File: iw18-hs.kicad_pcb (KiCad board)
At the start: 2 copper layers, 115 parts, among them J1 USB_C_Receptacle_USB2.0_14P, Q1 Q_NMOS_GSD, Q2 Q_NMOS_GDS, SW1 SW_SPST, SW2 SW_SPDT, U1 IV-18, U10 TXS0104EPW, U11 MAX811TEUS-T, U12 AT24CS08-STUM, U13 MQ-6, U14 BME680, U15 LSM6DS3, U2 BQ25895RTW, U3 ESP32-C6-WROOM-1, U4 LM1117DT-3.3, U5 MCP4017-xxxxLT, U6 TPS25751DREFR_C30169739, U7 LM3478MA, U8 USBLC6-2P6, U9 DRV8837

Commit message: Component changes, some new feature
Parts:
- removed C15: 10uF, Capacitor_SMD:CP_Elec_5x4.5
- added C52: 10uF, Capacitor_SMD:C_1206_3216Metric, F.Cu at (187.2, 128.0)
- added R6: 10k, Resistor_SMD:R_0805_2012Metric, F.Cu at (161.0, 136.5)
- added U16: 74LVC1G125, Package_TO_SOT_SMD:Texas_R-PDSO-G5_DCK-5, F.Cu at (161.1, 133.2)
- C13, C16, C51: value 150uF -> 100uF; footprint Capacitor_SMD:CP_Elec_5x4.5 -> Capacitor_SMD:C_1206_3216Metric
- C17, C21, C22, C24, C25, C32, C34: footprint Capacitor_SMD:C_0805_2012Metric -> Capacitor_SMD:C_0402_1005Metric
- C4: value 50uF -> 47uF
- D1: value SS14-DC -> SBA120CS-R1; footprint Diode_SMD:D_SMA -> Diode_SMD:D_SOD-323
- D4: value B3100BE-13 -> SDB160WS-AQ-DIO; footprint Diode_SMD:D_SMB -> Diode_SMD:D_SOD-323
- L1: value L -> 100uH; footprint Inductor_SMD:L_1812_4532Metric -> Inductor_SMD:L_0805_2012Metric
- L2: value 47uF -> 100uH
- L3: value 2.2uF -> 2.2uH; footprint Inductor_SMD:L_Bourns_SRP1038C_10.0x10.0mm -> Inductor_SMD:L_Taiyo-Yuden_NR-50xx
- Q2: footprint Package_TO_SOT_SMD:TO-263-2 -> Package_TO_SOT_SMD:TO-252-3_TabPin2
- R10: value 2.7k -> 10k
- R31, R32: footprint Resistor_SMD:R_0805_2012Metric -> Resistor_SMD:R_0402_1005Metric
- U4: footprint Package_TO_SOT_SMD:TO-252-3_TabPin2 -> Package_TO_SOT_SMD:SOT-223-3_TabPin2
- moved U13 106.1 mm to (64.6, 24.6)
- moved J1 97.5 mm to (28.9, 106.2), turned to -90 degrees
- moved R16 87.9 mm to (35.9, 102.7), turned to 0 degrees
- moved U8 87.6 mm to (35.9, 105.1), turned to 0 degrees
- moved R15 87.5 mm to (35.8, 107.7), turned to 0 degrees
- moved F1 87.4 mm to (35.9, 110.0), turned to 0 degrees
- moved C18 46.8 mm to (55.3, 141.6)
- moved C23 46.8 mm to (59.0, 137.1)
- moved R19 46.8 mm to (51.6, 137.1)
- moved R22 46.8 mm to (55.3, 137.1)
- moved R28 46.8 mm to (55.3, 139.3)
- moved R29 46.8 mm to (46.3, 138.9)
- moved R30 46.8 mm to (46.3, 141.1)
- moved BT1 46.8 mm to (50.0, 67.2)
- moved C19 46.8 mm to (48.5, 95.6)
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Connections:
- U3 pad 15: ETANOL_SENSOR_HEAT -> unconnected-(U3-GPIO9-Pad15)
- U3 pad 27: unconnected-(U3-GPIO2/ADC1_CH2-Pad27) -> ETANOL_SENSOR_HEAT
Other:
- board outline added: 40 x 120.8 mm

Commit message: plytka wip
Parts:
- added J2: Conn_02x10_Counter_Clockwise, Connector_PinHeader_2.54mm:PinHeader_2x10_P2.54mm_Vertical, F.Cu at (33.8, 67.0)
- added J3: Conn_02x10_Counter_Clockwise, Connector_PinSocket_2.54mm:PinSocket_2x10_P2.54mm_Horizontal, F.Cu at (33.6, 49.5)
- moved C51 222.4 mm to (36.0, 150.0)
- moved L1 221.1 mm to (34.8, 146.8)
- moved TP5 220.3 mm to (30.2, 149.8)
- moved C13 217.6 mm to (33.5, 150.0)
- moved C12 214.7 mm to (32.0, 153.8)
- moved U4 213.7 mm to (31.0, 159.5)
- moved C11 204.8 mm to (28.5, 153.2)
- moved C4 204.2 mm to (26.0, 153.2)
- moved TP4 154.8 mm to (49.7, 122.3), turned to 180 degrees
- moved C3 148.0 mm to (49.7, 119.0), turned to 90 degrees
- moved C14 144.7 mm to (62.2, 78.8), turned to -90 degrees
- moved U5 144.0 mm to (60.0, 79.0), turned to -90 degrees
- moved TP1 142.8 mm to (63.5, 83.8), turned to 90 degrees
- moved R10 141.6 mm to (48.2, 90.8)
- moved C52 140.7 mm to (53.7, 83.8), turned to 0 degrees
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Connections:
- net /. renamed /VFD/.
- net /A renamed /VFD/A
- net /B renamed /VFD/B
- net /C renamed /VFD/C
- net /D renamed /VFD/D
- net /D1 renamed /VFD/D1
- net /D2 renamed /VFD/D2
- net /D3 renamed /VFD/D3
- net /D4 renamed /VFD/D4
- net /D5 renamed /VFD/D5
- net /D6 renamed /VFD/D6
- net /D7 renamed /VFD/D7
- net /D8 renamed /VFD/D8
- net /D9 renamed /VFD/D9
- net /E renamed /VFD/E
- net /F renamed /VFD/F
- net /G renamed /VFD/G
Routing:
- net /VFD/D5: track 0.00 -> 83.9 mm, vias 0 -> 1
- net /VFD/D3: track 0.00 -> 73.9 mm, vias 0 -> 1
- net /VFD/D4: track 0.00 -> 65.4 mm, vias 0 -> 2
- net /VFD/D1: track 0.00 -> 63.1 mm, vias 0 -> 1
- net /VFD/D2: track 0.00 -> 52.4 mm, vias 0 -> 2
- net /VFD/F: track 0.00 -> 51.1 mm, vias 0 -> 2
- net /VFD/G: track 0.00 -> 40.5 mm, vias 0 -> 2
- net HEATER_A: track 0.00 -> 36.9 mm, vias 0 -> 2
- net /VFD/.: track 0.00 -> 35.9 mm, vias 0 -> 2
- net GND: track 0.00 -> 5.26 mm
- net Net-(U2-REGN): track 0.00 -> 2.28 mm
- net VSYS: track 0.00 -> 0.50 mm
- net Net-(SW2-B): track 0.00 -> 0.50 mm
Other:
- board size 40 x 120.8 mm -> 40 x 159.5 mm
- board text added: "Do ogarnięcia pozycjonowanie. na razie wys 18mm+10mm+10mm, szer 40mm czy aby na pewno dobra kolejnosc pinów? będziemy pewnie od tyłu robić."

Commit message: components moved
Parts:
- moved C39 6.26 mm to (84.3, 146.7)
- moved C40 6.26 mm to (84.2, 127.3)
- moved C41 6.26 mm to (84.9, 108.6)
- moved C45 6.26 mm to (84.4, 90.1)
- moved D3 6.26 mm to (79.9, 146.6)
- moved D5 6.26 mm to (79.9, 127.5)
- moved D6 6.26 mm to (80.2, 108.8)
- moved D7 6.26 mm to (80.0, 90.5)
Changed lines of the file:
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@@
 	(footprint "Capacitor_SMD:C_0805_2012Metric"
 		(layer "F.Cu")
-		(at 89.9 87.1 -90)
+		(at 84.4 90.1 -90)
 		(descr "Capacitor SMD 0805 (2012 Metric), square (rectangular) end terminal, IPC-7351 nominal, (Body size source: IPC-SM-782 page 76, https://www.pcb-3d.com/wordpress/wp-content/uploads/ipc-sm-782a_amendment_1_and_2.pdf, https://docs.google.com/spreadsheets/d/1BsfQQcO9C6DZCsRaXUlFlo91Tg2WpOkGARC1WS5S8t0/edit?usp=sharing)")
 		(tags "capacitor")
@@
 	(footprint "LED_SMD:LED_WS2812B_PLCC4_5.0x5.0mm_P3.2mm"
 		(layer "F.Cu")
-		(at 85.4 124.5 -90)
+		(at 79.9 127.5 -90)
 		(descr "5.0mm x 5.0mm Addressable RGB LED NeoPixel, https://cdn-shop.adafruit.com/datasheets/WS2812B.pdf")
 		(tags "LED RGB NeoPixel PLCC-4 5050")
@@
 	(footprint "LED_SMD:LED_WS2812B_PLCC4_5.0x5.0mm_P3.2mm"
 		(layer "F.Cu")
-		(at 85.5 87.5 -90)
+		(at 80 90.5 -90)
 		(descr "5.0mm x 5.0mm Addressable RGB LED NeoPixel, https://cdn-shop.adafruit.com/datasheets/WS2812B.pdf")
 		(tags "LED RGB NeoPixel PLCC-4 5050")
@@
 	(footprint "Capacitor_SMD:C_0805_2012Metric"
 		(layer "F.Cu")
-		(at 89.8 143.7 -90)
+		(at 84.3 146.7 -90)
 		(descr "Capacitor SMD 0805 (2012 Metric), square (rectangular) end terminal, IPC-7351 nominal, (Body size source: IPC-SM-782 page 76, https://www.pcb-3d.com/wordpress/wp-content/uploads/ipc-sm-782a_amendment_1_and_2.pdf, https://docs.google.com/spreadsheets/d/1BsfQQcO9C6DZCsRaXUlFlo91Tg2WpOkGARC1WS5S8t0/edit?usp=sharing)")
 		(tags "capacitor")
@@
 	(footprint "LED_SMD:LED_WS2812B_PLCC4_5.0x5.0mm_P3.2mm"
 		(layer "F.Cu")
-		(at 85.75 105.85 -90)
+		(at 80.25 108.85 -90)
 		(descr "5.0mm x 5.0mm Addressable RGB LED NeoPixel, https://cdn-shop.adafruit.com/datasheets/WS2812B.pdf")
 		(tags "LED RGB NeoPixel PLCC-4 5050")
@@
 	(footprint "Capacitor_SMD:C_0805_2012Metric"
 		(layer "F.Cu")
-		(at 90.4 105.6 -90)
+		(at 84.9 108.6 -90)
 		(descr "Capacitor SMD 0805 (2012 Metric), square (rectangular) end terminal, IPC-7351 nominal, (Body size source: IPC-SM-782 page 76, https://www.pcb-3d.com/wordpress/wp-content/uploads/ipc-sm-782a_amendment_1_and_2.pdf, https://docs.google.com/spreadsheets/d/1BsfQQcO9C6DZCsRaXUlFlo91Tg2WpOkGARC1WS5S8t0/edit?usp=sharing)")
 		(tags "capacitor")
@@
 	(footprint "Capacitor_SMD:C_0805_2012Metric"
 		(layer "F.Cu")
-		(at 89.65 124.3 -90)
+		(at 84.15 127.3 -90)
 		(descr "Capacitor SMD 0805 (2012 Metric), square (rectangular) end terminal, IPC-7351 nominal, (Body size source: IPC-SM-782 page 76, https://www.pcb-3d.com/wordpress/wp-content/uploads/ipc-sm-782a_amendment_1_and_2.pdf, https://docs.google.com/spreadsheets/d/1BsfQQcO9C6DZCsRaXUlFlo91Tg2WpOkGARC1WS5S8t0/edit?usp=sharing)")
 		(tags "capacitor")
@@
 	(footprint "LED_SMD:LED_WS2812B_PLCC4_5.0x5.0mm_P3.2mm"
 		(layer "F.Cu")
-		(at 85.4 143.55 -90)
+		(at 79.9 146.55 -90)
 		(descr "5.0mm x 5.0mm Addressable RGB LED NeoPixel, https://cdn-shop.adafruit.com/datasheets/WS2812B.pdf")
 		(tags "LED RGB NeoPixel PLCC-4 5050")
@@
 	)
 	(gr_text "Do ogarnięcia pozycjonowanie. na razie wys 18mm+10mm+10mm, szer 40mm\nczy aby na pewno dobra kolejnosc pinów? będziemy pewnie od tyłu robić."
-		(at 8.75 58.75 0)
+		(at 13 59.75 0)
 		(layer "F.Fab")
 		(effects

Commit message: Do compoent placing
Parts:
- added BT2: 247, 247:BAT_247, B.Cu at (111.4, 101.6)
- added J4: Conn_02x08_Odd_Even, Connector_PinHeader_2.54mm:PinHeader_2x08_P2.54mm_Vertical, F.Cu at (214.2, 110.3)
- added J5: Conn_02x08_Odd_Even, Connector_PinHeader_2.54mm:PinHeader_2x08_P2.54mm_Vertical, F.Cu at (208.1, 110.3)
- BT1: value Battery_Cell -> 247; footprint Battery:BatteryHolder_MPD_BH-18650-PC -> 247:BAT_247
- U13: moved to B.Cu
- moved C26 165.7 mm to (177.9, 93.3), turned to 180 degrees
- moved U3 159.0 mm to (189.9, 100.3), turned to 0 degrees
- moved C28 148.6 mm to (164.8, 109.9), turned to 0 degrees
- moved U8 141.8 mm to (175.2, 89.6)
- moved R30 140.2 mm to (169.6, 95.7), turned to 0 degrees
- moved U13 139.4 mm to (241.1, 105.2), turned to 90 degrees
- moved C4 137.1 mm to (153.7, 103.4)
- moved C11 136.7 mm to (155.8, 103.4)
- moved R5 136.6 mm to (224.7, 110.2), turned to 0 degrees
- moved R7 136.2 mm to (177.9, 113.3), turned to 90 degrees
- moved R29 136.2 mm to (166.1, 95.7)
- moved U11 136.1 mm to (172.9, 96.5), turned to 180 degrees
- moved R26 134.7 mm to (177.9, 109.9), turned to -90 degrees
- moved C12 133.7 mm to (158.0, 108.9)
- moved Q1 131.6 mm to (224.2, 106.6), turned to 180 degrees
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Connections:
- SW2 pad 3: Net-(BT1-+) -> Net-(SW2-C)
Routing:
- net /VFD/D5: track 83.9 -> 0.00 mm, vias 1 -> 0
- net /VFD/D3: track 73.9 -> 0.00 mm, vias 1 -> 0
- net /VFD/D4: track 65.4 -> 0.00 mm, vias 2 -> 0
- net /VFD/D1: track 63.1 -> 0.00 mm, vias 1 -> 0
- net /VFD/D2: track 52.4 -> 0.00 mm, vias 2 -> 0
- net /VFD/F: track 51.1 -> 0.00 mm, vias 2 -> 0
- net /VFD/G: track 40.5 -> 0.00 mm, vias 2 -> 0
- net HEATER_A: track 36.9 -> 0.00 mm, vias 2 -> 0
- net /VFD/.: track 35.9 -> 0.00 mm, vias 2 -> 0
- net GND: track 5.26 -> 0.00 mm
- net Net-(U2-REGN): track 2.28 -> 0.00 mm
- net VSYS: track 0.50 -> 0.00 mm
- net Net-(SW2-B): track 0.50 -> 0.00 mm
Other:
- board size 40 x 159.5 mm -> 204.4 x 40 mm
- board text removed: "Periph"
- board text removed: "Power"

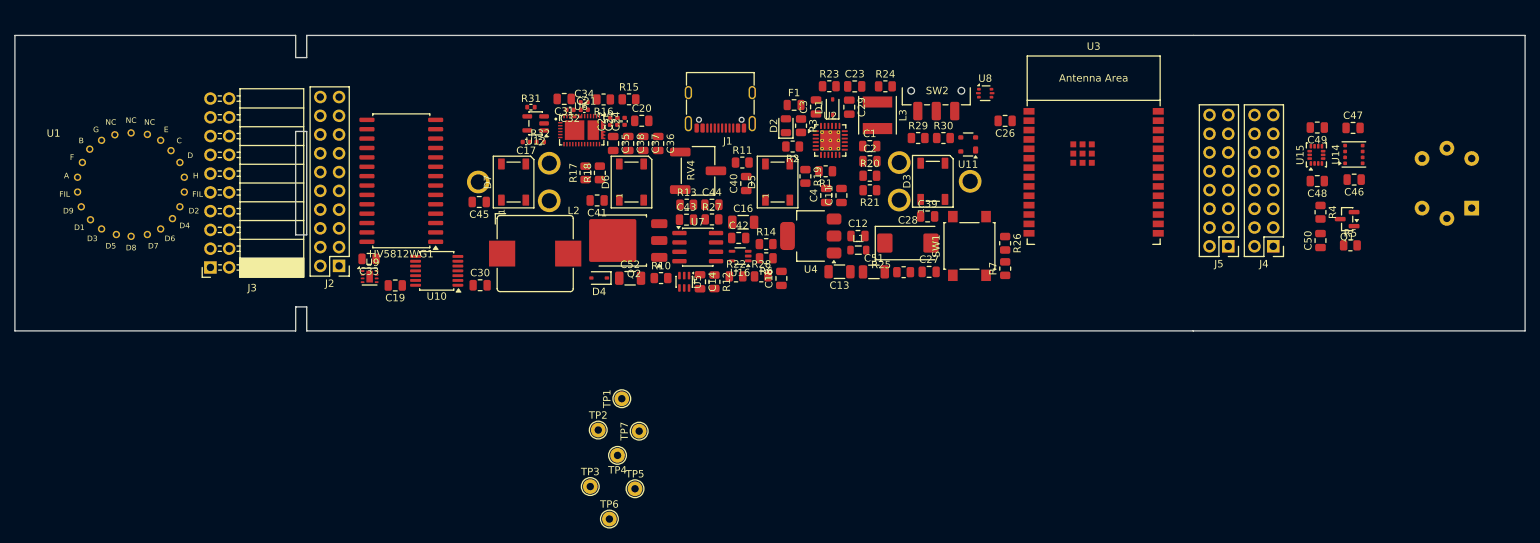
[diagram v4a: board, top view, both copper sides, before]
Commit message: Refine board
* Add UART connector for chaining and controll
* shrink the board
workspace 1 output DP-6
* allow for pd controller eeprom programming
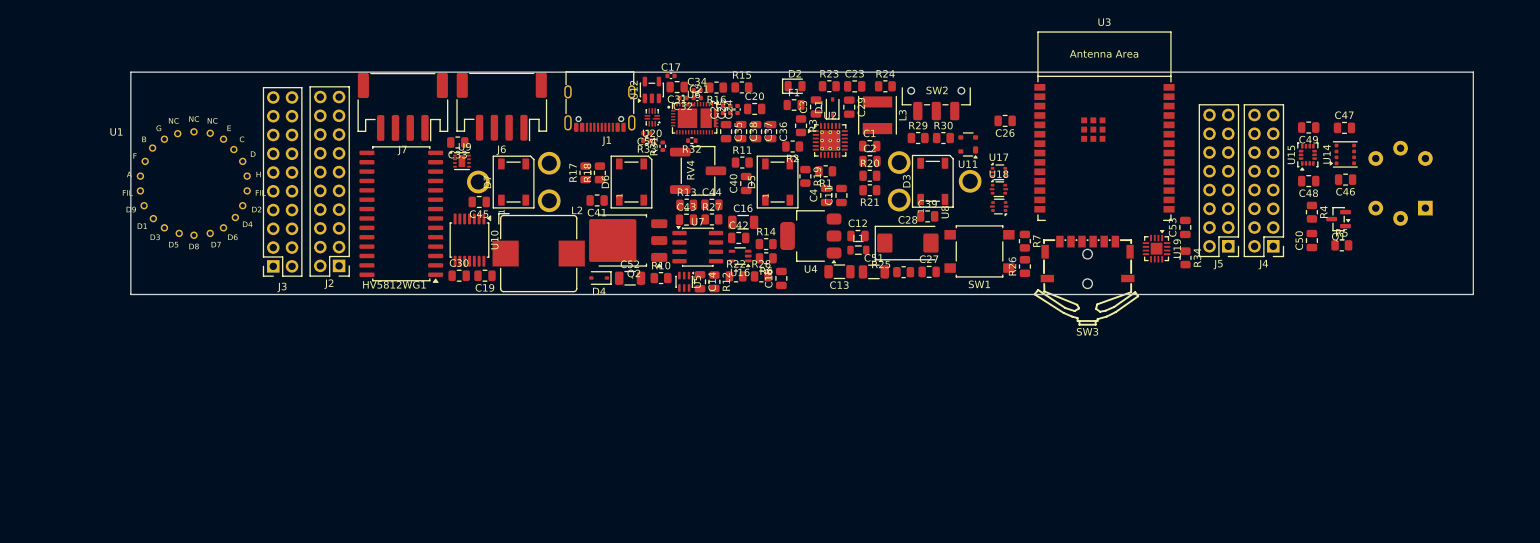
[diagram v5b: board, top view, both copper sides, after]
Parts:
- removed TP1, TP2, TP3, TP4, TP5, TP6, TP7: TestPoint_Probe, TestPoint:TestPoint_THTPad_D2.0mm_Drill1.0mm
- added C53: 100nF, Capacitor_SMD:C_0805_2012Metric, F.Cu at (202.3, 107.8)
- added C54: 100nF, Capacitor_SMD:C_0402_1005Metric, F.Cu at (129.4, 95.0)
- added J6: Conn_01x04_MountingPin, Connector_JST:JST_PH_S4B-PH-SM4-TB_1x04-1MP_P2.00mm_Horizontal, F.Cu at (109.8, 91.4)
- added J7: Conn_01x04_MountingPin, Connector_JST:JST_PH_S4B-PH-SM4-TB_1x04-1MP_P2.00mm_Horizontal, F.Cu at (96.4, 91.4)
- added R33: 10k, Resistor_SMD:R_0402_1005Metric, F.Cu at (129.4, 96.0)
- added R34: 10k, Resistor_SMD:R_0805_2012Metric, F.Cu at (202.3, 111.9)
- added SW3: SLLB120200, JLCImport:SLLB120200, F.Cu at (189.1, 112.2)
- added U17: USBLC6-2P6, Package_TO_SOT_SMD:SOT-666, F.Cu at (177.1, 100.3)
- added U18: USBLC6-2P6, Package_TO_SOT_SMD:SOT-666, F.Cu at (177.1, 102.6)
- added U19: PCF8574RGTR, Package_DFN_QFN:WQFN-16-1EP_3x3mm_P0.5mm_EP1.6x1.6mm, F.Cu at (198.4, 110.6)
- added U20: TMUX154ERSW, Package_DFN_QFN:UQFN-10_1.4x1.8mm_P0.4mm, F.Cu at (130.1, 92.9)
- J3: footprint Connector_PinSocket_2.54mm:PinSocket_2x10_P2.54mm_Horizontal -> Connector_PinSocket_2.54mm:PinSocket_2x10_P2.54mm_Vertical
- moved C17 21.5 mm to (132.7, 87.2), turned to 0 degrees
- moved R32 20.5 mm to (135.5, 96.0), turned to 180 degrees
- moved U9 20.0 mm to (104.4, 98.8)
- moved C33 19.8 mm to (103.8, 96.3)
- moved R31 18.6 mm to (131.6, 96.8), turned to 90 degrees
- moved U12 16.4 mm to (130.1, 89.2), turned to 90 degrees
- moved J1 16.3 mm to (123.1, 90.5)
- moved U8 15.5 mm to (177.1, 104.9), turned to 180 degrees
- moved C20 15.4 mm to (144.0, 91.7)
- moved C24 15.4 mm to (141.7, 91.8)
- moved C25 15.4 mm to (140.7, 91.8)
- moved C32 15.4 mm to (134.3, 90.2)
- moved C34 15.4 mm to (136.2, 89.2)
- moved C36 15.4 mm to (146.2, 94.8)
- moved C38 15.4 mm to (142.2, 94.8)
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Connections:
- C18 pad 1: Net-(U3-MTDI/GPIO5/ADC1_CH5) -> Net-(U3-GPIO3/ADC1_CH3)
- C23 pad 1: Net-(U3-MTMS/GPIO4/ADC1_CH4) -> Net-(U3-GPIO2/ADC1_CH2)
- Q1 pad 2: Net-(Q1-S) -> GND
- Q1 pad 3: +5V -> Net-(Q1-D)
- R19 pad 2: GND -> +3.3V
- R22 pad 2: Net-(U3-MTDI/GPIO5/ADC1_CH5) -> Net-(U3-GPIO3/ADC1_CH3)
- R23 pad 2: Net-(U3-MTMS/GPIO4/ADC1_CH4) -> Net-(U3-GPIO2/ADC1_CH2)
- R24 pad 1: Net-(U3-MTMS/GPIO4/ADC1_CH4) -> Net-(U3-GPIO2/ADC1_CH2)
- R28 pad 1: Net-(U3-MTDI/GPIO5/ADC1_CH5) -> Net-(U3-GPIO3/ADC1_CH3)
- R29 pad 2: Net-(U3-MTCK/GPIO6/ADC1_CH6) -> Net-(U3-MTMS/GPIO4/ADC1_CH4)
- R30 pad 1: Net-(U3-MTCK/GPIO6/ADC1_CH6) -> Net-(U3-MTMS/GPIO4/ADC1_CH4)
- R31 pad 2: PD_EEPROM_SDA -> Net-(U20-A0)
- R32 pad 2: PD_EEPROM_SCL -> Net-(U20-B0)
- U12 pad 1: PD_EEPROM_SCL -> Net-(U12-SCL)
- U12 pad 3: PD_EEPROM_SDA -> Net-(U12-SDA)
- U13 pad 2: Net-(Q1-S) -> +5V
- U13 pad 5: GND -> Net-(Q1-D)
- U15 pad 9: IMU_INT1 -> unconnected-(U15-INT2-Pad9)
- U3 pad 10: unconnected-(U3-GPIO8-Pad10) -> ETANOL_SENSOR_HEAT
- U3 pad 15: unconnected-(U3-GPIO9-Pad15) -> WS2812B_DATA
- U3 pad 20: IMU_INT0 -> UART1_TX
- U3 pad 21: IMU_INT1 -> UART1_RX
- U3 pad 23: WS2812B_DATA -> PROGRAM_PD_CONTROLLER
- U3 pad 24: unconnected-(U3-U0RXD/GPIO17-Pad24) -> UART0_RX
- U3 pad 25: unconnected-(U3-U0TXD/GPIO16-Pad25) -> UART0_TX
- U3 pad 26: ETANOL_SENSE_ADC -> Net-(U3-GPIO3/ADC1_CH3)
- U3 pad 27: ETANOL_SENSOR_HEAT -> Net-(U3-GPIO2/ADC1_CH2)
- U3 pad 5: Net-(U3-MTDI/GPIO5/ADC1_CH5) -> CHG_INT
- U3 pad 6: Net-(U3-MTCK/GPIO6/ADC1_CH6) -> JOYSTICK_INT
- U3 pad 7: CHG_INT -> unconnected-(U3-MTDO/GPIO7-Pad7)
- U3 pad 8: unconnected-(U3-GPIO0/ADC1_CH0/XTAL_32K_P-Pad8) -> IMU_INT0
- U3 pad 9: unconnected-(U3-GPIO1/ADC1_CH1/XTAL_32K_N-Pad9) -> ETANOL_SENSE_ADC
- U6 pad 18: USB_PD_INT -> CHG_INT
- U6 pad 8: PD_EEPROM_SDA -> Net-(U20-A0)
- U6 pad 9: PD_EEPROM_SCL -> Net-(U20-B0)
- U8 pad 1: USB_D+ -> PRE_USB_D+
- U8 pad 3: USB_D- -> PRE_USB_D-
- U8 pad 4: PRE_USB_D- -> USB_D-
- U8 pad 6: PRE_USB_D+ -> USB_D+
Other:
- board size 204.4 x 40 mm -> 181.7 x 30.1 mm

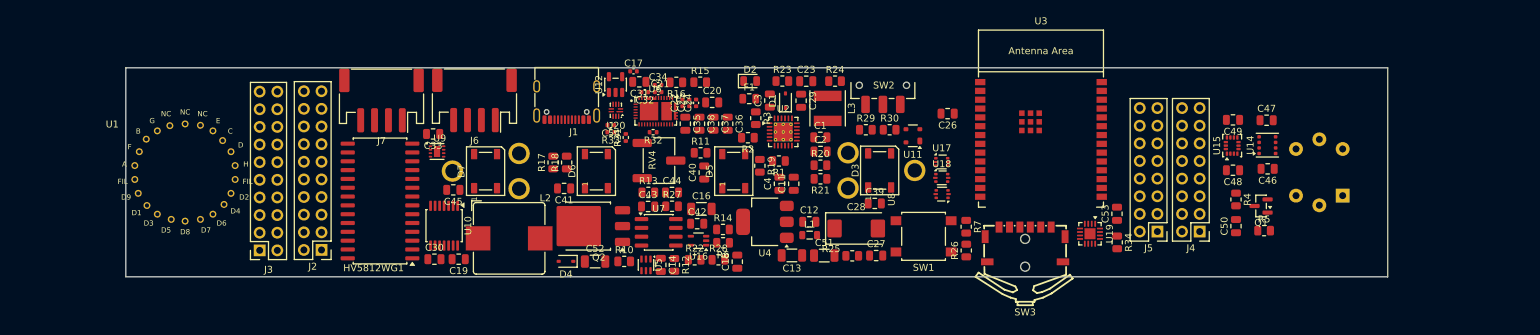
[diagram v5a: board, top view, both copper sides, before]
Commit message: Add mounting holes and put test points
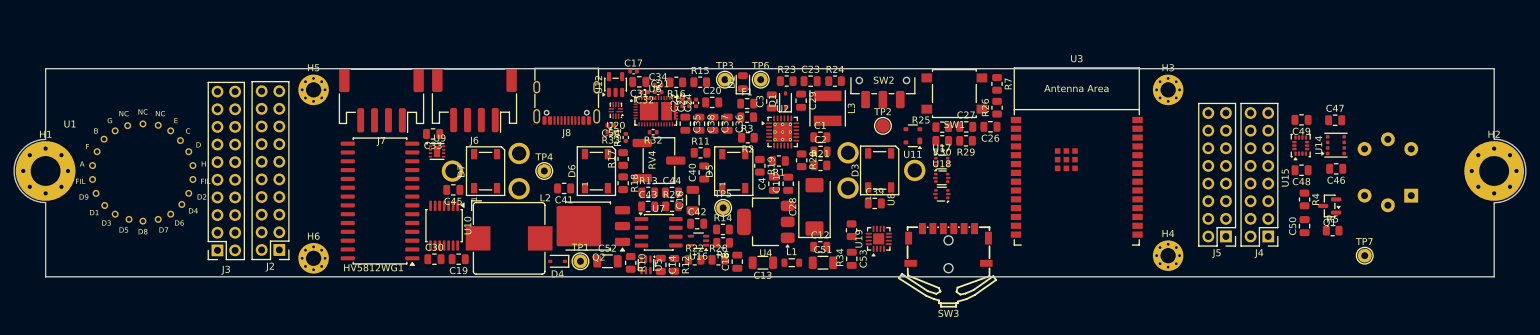
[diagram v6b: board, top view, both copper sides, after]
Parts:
- removed J1: USB_C_Receptacle_USB2.0_14P, Connector_USB:USB_C_Receptacle_G-Switch_GT-USB-7010ASV
- added H1: MountingHole_Pad, MountingHole:MountingHole_4.3mm_M4_Pad_Via, F.Cu at (48.0, 101.6)
- added H2: MountingHole_Pad, MountingHole:MountingHole_4.3mm_M4_Pad_Via, F.Cu at (256.6, 101.6)
- added H3: MountingHole_Pad, MountingHole:MountingHole_2.2mm_M2_Pad_Via, F.Cu at (209.7, 89.9)
- added H4: MountingHole_Pad, MountingHole:MountingHole_2.2mm_M2_Pad_Via, F.Cu at (209.7, 113.8)
- added H5: MountingHole_Pad, MountingHole:MountingHole_2.2mm_M2_Pad_Via, F.Cu at (86.6, 89.9)
- added H6: MountingHole_Pad, MountingHole:MountingHole_2.2mm_M2_Pad_Via, F.Cu at (86.6, 114.2)
- added J8: USB_C_Receptacle_USB2.0_16P, Connector_USB:USB_C_Receptacle_G-Switch_GT-USB-7010ASV, F.Cu at (123.1, 90.6)
- added TP1: TestPoint_Probe, TestPoint:TestPoint_THTPad_D2.0mm_Drill1.0mm, F.Cu at (125.0, 114.6)
- added TP2: TestPoint_Probe, TestPoint:TestPoint_Pad_D2.0mm, F.Cu at (168.6, 95.1)
- added TP3: TestPoint_Probe, TestPoint:TestPoint_THTPad_D2.0mm_Drill1.0mm, F.Cu at (145.8, 88.4)
- added TP4: TestPoint_Probe, TestPoint:TestPoint_THTPad_D2.0mm_Drill1.0mm, F.Cu at (119.8, 101.6)
- added TP5: TestPoint_Probe, TestPoint:TestPoint_THTPad_D2.0mm_Drill1.0mm, F.Cu at (145.6, 106.9)
- added TP6: TestPoint_Probe, TestPoint:TestPoint_THTPad_D2.0mm_Drill1.0mm, F.Cu at (151.0, 88.4)
- added TP7: TestPoint_Probe, TestPoint:TestPoint_THTPad_D2.0mm_Drill1.0mm, F.Cu at (238.0, 113.8)
- moved C53 38.7 mm to (164.1, 114.3), turned to -90 degrees
- moved R34 38.3 mm to (164.1, 110.1), turned to 90 degrees
- moved U19 30.4 mm to (168.0, 111.4), turned to 90 degrees
- moved C27 22.6 mm to (180.6, 95.2)
- moved R25 22.6 mm to (177.1, 95.3)
- moved R26 21.0 mm to (185.0, 92.5)
- moved SW1 21.0 mm to (178.9, 90.4)
- moved R7 21.0 mm to (185.0, 89.1)
- moved R29 14.5 mm to (180.6, 97.3), turned to 180 degrees
- moved SW3 11.0 mm to (178.1, 112.4)
- moved R17 10.1 mm to (131.2, 99.9)
- moved J4 9.90 mm to (224.1, 111.0)
- moved J5 9.90 mm to (218.0, 111.0)
- moved C50 9.87 mm to (229.3, 109.5)
- moved R4 9.87 mm to (229.3, 105.7)
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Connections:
- BT1 pad 1_1: Net-(SW2-C) -> Net-(SW2-A)
- BT1 pad 1_2: Net-(SW2-C) -> Net-(SW2-A)
- BT1 pad 1_3: Net-(SW2-C) -> Net-(SW2-A)
- SW2 pad 1: unconnected-(SW2-A-Pad1) -> Net-(SW2-A)
- SW2 pad 3: Net-(SW2-C) -> unconnected-(SW2-C-Pad3)
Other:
- board size 181.7 x 30.1 mm -> 217.7 x 30 mm
